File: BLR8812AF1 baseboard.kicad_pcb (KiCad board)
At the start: 2 copper layers, 38 x 38 mm, 24 parts, among them U1 MP2307DN, U2 USBLC6-2SC6, U3 BL-R8812AF1, X1 TYPE-C-31-M-12

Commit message: Working on board
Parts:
- added MH1: MountingHole, MountingHole:MountingHole_2.2mm_M2, F.Cu at (52.9, 62.2)
- added MH2: MountingHole, MountingHole:MountingHole_2.2mm_M2, F.Cu at (52.9, 28.8)
- added MH3: MountingHole, MountingHole:MountingHole_2.2mm_M2, F.Cu at (86.4, 28.8)
- added MH4: MountingHole, MountingHole:MountingHole_2.2mm_M2, F.Cu at (86.4, 62.2)
- added X2: ~, ULF:TH_1.7_1.7_1, F.Cu at (69.0, 28.2)
- added X3: ~, ULF:TH_1_1_0.65, F.Cu at (60.5, 40.3)
- added X4: ~, ULF:TH_1_1_0.65, F.Cu at (60.5, 38.4)
- added X5: ~, ULF:TH_1.7_1.7_1, F.Cu at (69.0, 35.1)
- added X6: ~, ULF:TH_1_1_0.65, F.Cu at (60.5, 42.2)
- C1, C2: value 10u -> 22u
- L1: footprint PCM_Inductor_SMD_AKL:L_7.3x7.3_H4.5 -> Inductor_SMD:L_SXN_SMDRI62
- moved U3 41.5 mm to (56.1, 61.3)
- moved R7 23.1 mm to (52.7, 57.4)
- moved C2 19.4 mm to (72.4, 31.6)
- moved U1 19.2 mm to (77.3, 30.7)
- moved C6 19.1 mm to (72.4, 28.5)
- moved C4 19.1 mm to (82.0, 28.8)
- moved R8 19.1 mm to (80.3, 34.9)
- moved C7 19.1 mm to (82.1, 31.4)
- moved C5 19.1 mm to (82.1, 32.6)
- moved C8 19.1 mm to (79.8, 39.7)
- moved R2 19.1 mm to (82.1, 30.1)
- moved R3 19.1 mm to (82.1, 33.9)
- moved R9 19.1 mm to (79.0, 34.9)
- moved L1 19.1 mm to (73.9, 38.3)
- moved C1 18.9 mm to (69.0, 31.6)
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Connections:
- net Net-(X1-DN1) renamed /DN
- net Net-(X1-DP1) renamed /DP

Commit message: Completed placing
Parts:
- moved X6 6.46 mm to (58.9, 36.0)
- moved R5 5.28 mm to (52.1, 43.2), turned to -90 degrees
- moved R4 2.98 mm to (53.6, 43.2), turned to -90 degrees
- moved D1 2.69 mm to (65.4, 37.7), turned to -90 degrees
- moved R6 1.63 mm to (65.4, 40.5), turned to -90 degrees
- moved R7 0.49 mm to (52.9, 56.9)
- moved U3 0.45 mm to (56.1, 60.8)
- moved MH1 0.40 mm to (52.6, 62.5)
- moved MH4 0.40 mm to (86.6, 62.5)
- moved MH2 0.40 mm to (52.6, 28.5)
- moved MH3 0.40 mm to (86.6, 28.5)
- moved R1 0.30 mm to (53.8, 33.0)
- moved C9 0.20 mm to (82.4, 39.7)
- moved C3 0.20 mm to (53.8, 35.5)
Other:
- outline, holes or cut-outs redrawn
- board text added: "ADD PADS FOR USB to CAM CONNECTION AND POWERRRRRR Ensure holes size"
- board text removed: "ADD PADS FOR USB to CAM CONNECTION AND POWERRRRRR"

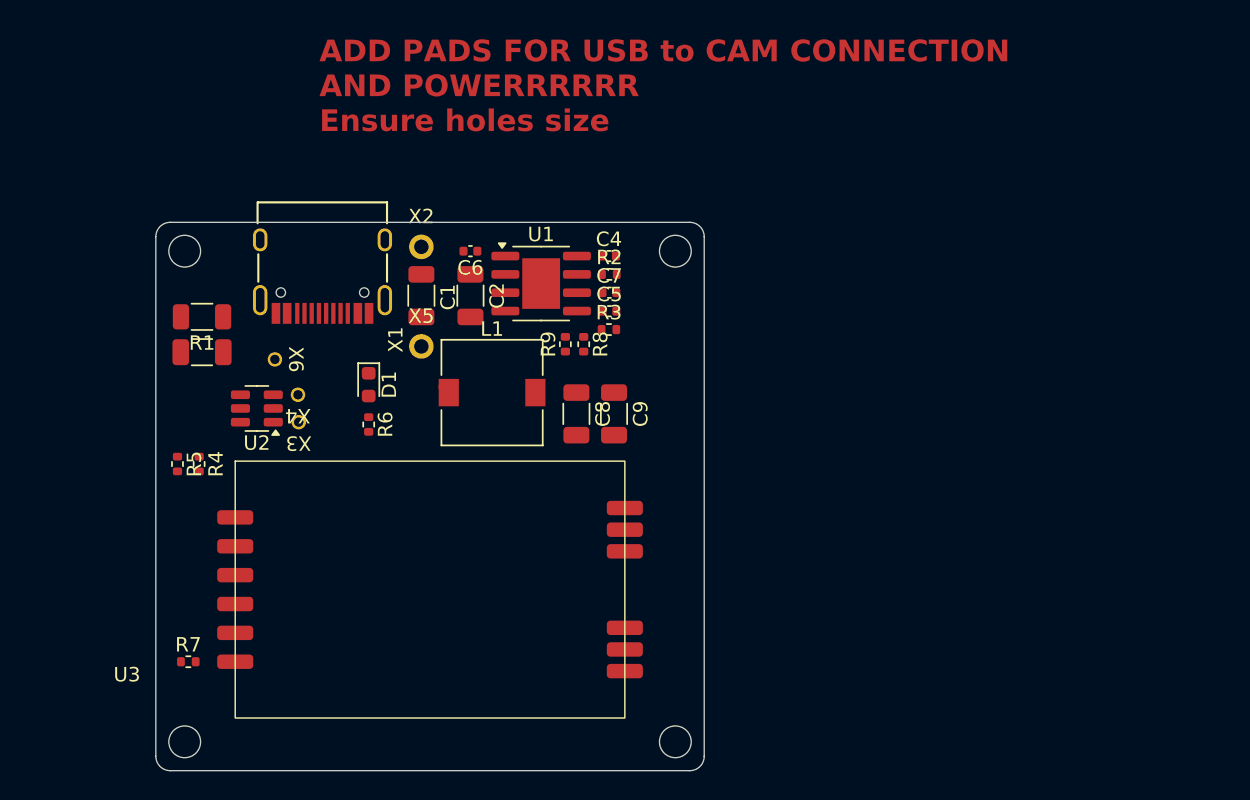
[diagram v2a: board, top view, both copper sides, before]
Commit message: changed DC-DC
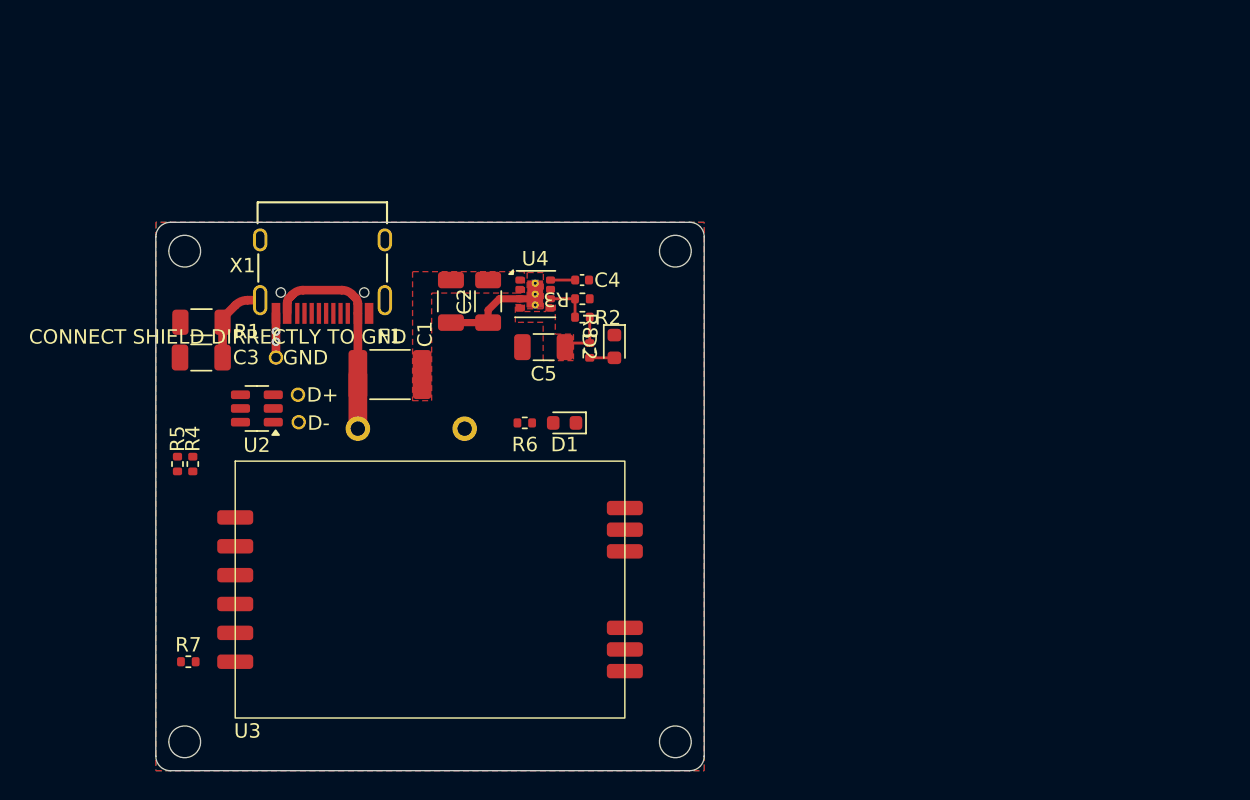
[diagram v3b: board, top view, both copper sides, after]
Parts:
- removed C6: 10n, Capacitor_SMD:C_0402_1005Metric
- removed C7: DNP, Capacitor_SMD:C_0402_1005Metric
- removed C8, C9: 22u, Capacitor_SMD:C_1206_3216Metric
- removed L1: 2uH, Inductor_SMD:L_SXN_SMDRI62
- removed R9: 10k, Resistor_SMD:R_0402_1005Metric
- removed U1: MP2307DN, Package_SO:SOIC-8-1EP_3.9x4.9mm_P1.27mm_EP2.62x3.51mm
- added D2: DNP, LED_SMD:LED_0603_1608Metric, F.Cu at (82.4, 35.1)
- added F1: MF-MSMF110-2, Fuse:Fuse_1812_4532Metric_Pad1.30x3.40mm_HandSolder, F.Cu at (66.9, 37.0)
- added U4: TPS82130, Package_LGA:Texas_SIL0008D_MicroSiP-8-1EP_2.8x3mm_P0.65mm_EP1.1x1.9mm_ThermalVias, F.Cu at (76.9, 31.4)
- C4: value 0.1u -> 430p
- C5: value 3.9n -> 22u; footprint Capacitor_SMD:C_0402_1005Metric -> Capacitor_SMD:C_1206_3216Metric
- R2: value 100k -> 309k
- R3: value 6k8 -> 100k
- R8: value 26k1 -> DNP
- moved D1 13.8 mm to (79.0, 40.4), turned to 180 degrees
- moved X2 13.3 mm to (64.6, 40.8)
- moved R6 10.8 mm to (76.2, 40.4), turned to 180 degrees
- moved X5 6.44 mm to (72.0, 40.8)
- moved C5 5.19 mm to (77.5, 35.1), turned to 180 degrees
- moved R2 3.51 mm to (80.2, 33.0)
- moved R3 2.82 mm to (80.2, 31.8), turned to 180 degrees
- moved C4 2.50 mm to (80.2, 30.5)
- moved C1 2.09 mm to (71.1, 31.9)
- moved C2 1.29 mm to (73.7, 31.9)
- moved R8 0.60 mm to (80.7, 35.3), turned to 90 degrees
- moved R4 0.44 mm to (53.2, 43.2)
- moved R1 0.38 mm to (53.8, 33.4)
- moved C3 0.37 mm to (53.8, 35.8)
- moved X6 0.15 mm to (59.0, 35.8)
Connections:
- net Net-(R4-Pad1) renamed /D1_P
- net Net-(R5-Pad1) renamed /D1_N
- net Net-(U3-DN) renamed /D2_N
- net Net-(U3-DP) renamed /D2_P
- C1 pad 1: VBUS -> /Vin
- C2 pad 1: VBUS -> /Vin
- C5 pad 1: Net-(U1-COMP) -> 3.3V
- C5 pad 2: Net-(C5-Pad2) -> GND
- R2 pad 1: Net-(U1-EN) -> Net-(U4-FB)
- R2 pad 2: VBUS -> 3.3V
- R3 pad 2: Net-(C5-Pad2) -> Net-(U4-FB)
- R8 pad 2: 3V3 -> 3.3V
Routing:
- net VBUS: track 0.00 -> 15.2 mm
- net GND: track 0.00 -> 10.2 mm, vias 0 -> 2
- net Net-(C3-Pad1): track 0.00 -> 5.80 mm
- net 3.3V: track 0.00 -> 3.63 mm
- net Net-(U4-FB): track 0.00 -> 2.97 mm
- net Net-(U4-SS/TR): track 0.00 -> 1.71 mm
- net Net-(D2-A): track 0.00 -> 1.71 mm
- added copper zone on F.Cu, net /Vin
- added copper zone on F.Cu, net 3.3V
- added copper zone on B.Cu, net GND
- added copper zone on F.Cu, net GND
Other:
- board text added: "CONNECT SHIELD DIRRECTLY TO GND"
- board text added: "D+"
- board text added: "D-"
- board text added: "GND"
- board text removed: "ADD PADS FOR USB to CAM CONNECTION AND POWERRRRRR Ensure holes size"

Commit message: almost done
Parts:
- removed the C3 at (53.8, 35.8)
- added C5: 22u, Capacitor_SMD:C_1206_3216Metric, F.Cu at (53.3, 56.4)
- added Q1: AO3401A, Package_TO_SOT_SMD:SOT-23, F.Cu at (72.3, 37.0)
- R1: value 1M -> 10k; footprint Resistor_SMD:R_1206_3216Metric -> Resistor_SMD:R_0402_1005Metric
- moved R1 22.4 mm to (75.7, 38.0), turned to 90 degrees
- moved D1 18.7 mm to (60.3, 38.7)
- moved R4 18.7 mm to (57.6, 38.7)
- moved R5 9.37 mm to (60.5, 62.4), turned to 180 degrees
- moved X3 8.33 mm to (53.4, 34.0), turned to -90 degrees
- moved X2 8.19 mm to (55.3, 34.0), turned to -90 degrees
- moved U1 3.99 mm to (54.4, 37.1), turned to -90 degrees
- moved X4 2.52 mm to (57.2, 34.0)
- moved R3 1.77 mm to (52.5, 45.0)
- moved R2 1.77 mm to (53.5, 45.0)
- renumbered C4 to C3, C5 to C4, R4 to R2, R5 to R3, R6 to R4, R7 to R5, R3 to R6, R2 to R7, U2 to U1, U3 to U2, U4 to U3, X3 to X2, X4 to X3, X6 to X4, X2 to X5, X5 to X6
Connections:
- net VBUS renamed +VBUS
- C4 pad 1: 3.3V -> +3.3V
- F1 pad 2: /Vin -> Net-(Q1-S)
- R1 pad 1: Net-(C3-Pad1) -> GND
- R1 pad 2: GND -> Net-(Q1-G)
- R7 pad 2: 3.3V -> +3.3V
- R8 pad 2: 3.3V -> +3.3V
- U2 pad 2: 3V3 -> +3.3V
- U3 pad 4: 3.3V -> +3.3V
- U3 pad 5: 3.3V -> +3.3V
- X1 pad SHIELD: Net-(C3-Pad1) -> GND
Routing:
- net +3.3V: track 0.00 -> 51.7 mm, vias 0 -> 4
- net /DN: track 0.00 -> 18.1 mm
- net /DP: track 0.00 -> 17.5 mm
- net /D2_N: track 0.00 -> 9.97 mm
- net /D2_P: track 0.00 -> 9.26 mm
- net /Vin: track 0.00 -> 8.87 mm, vias 0 -> 5
- net +VBUS: track 15.2 -> 24.0 mm
- net /D1_P: track 0.00 -> 7.25 mm
- net /D1_N: track 0.00 -> 7.25 mm
- net Net-(C3-Pad1): track 5.80 -> 0.00 mm
- net Net-(Q1-G): track 0.00 -> 3.68 mm
- net 3.3V: track 3.63 -> 0.00 mm
- net GND: track 10.2 -> 10.9 mm, vias 2 -> 6
- added copper zone on F.Cu, net +3.3V
- added copper zone on F.Cu, net Net-(Q1-S)
- removed copper zone on F.Cu, net 3.3V
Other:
- board text added: "+5V"
- board text removed: "CONNECT SHIELD DIRRECTLY TO GND"

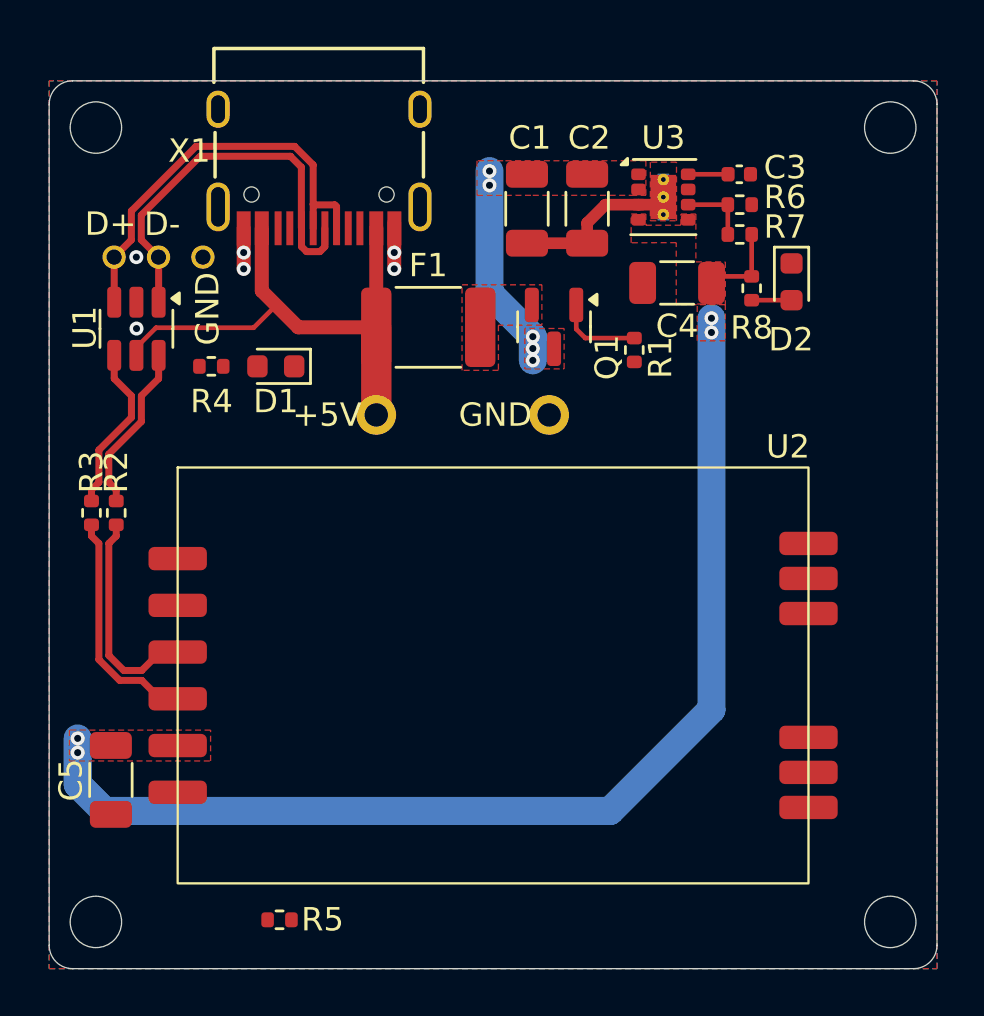
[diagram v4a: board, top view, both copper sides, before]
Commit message: Done placing and routing, need to add stiching vias
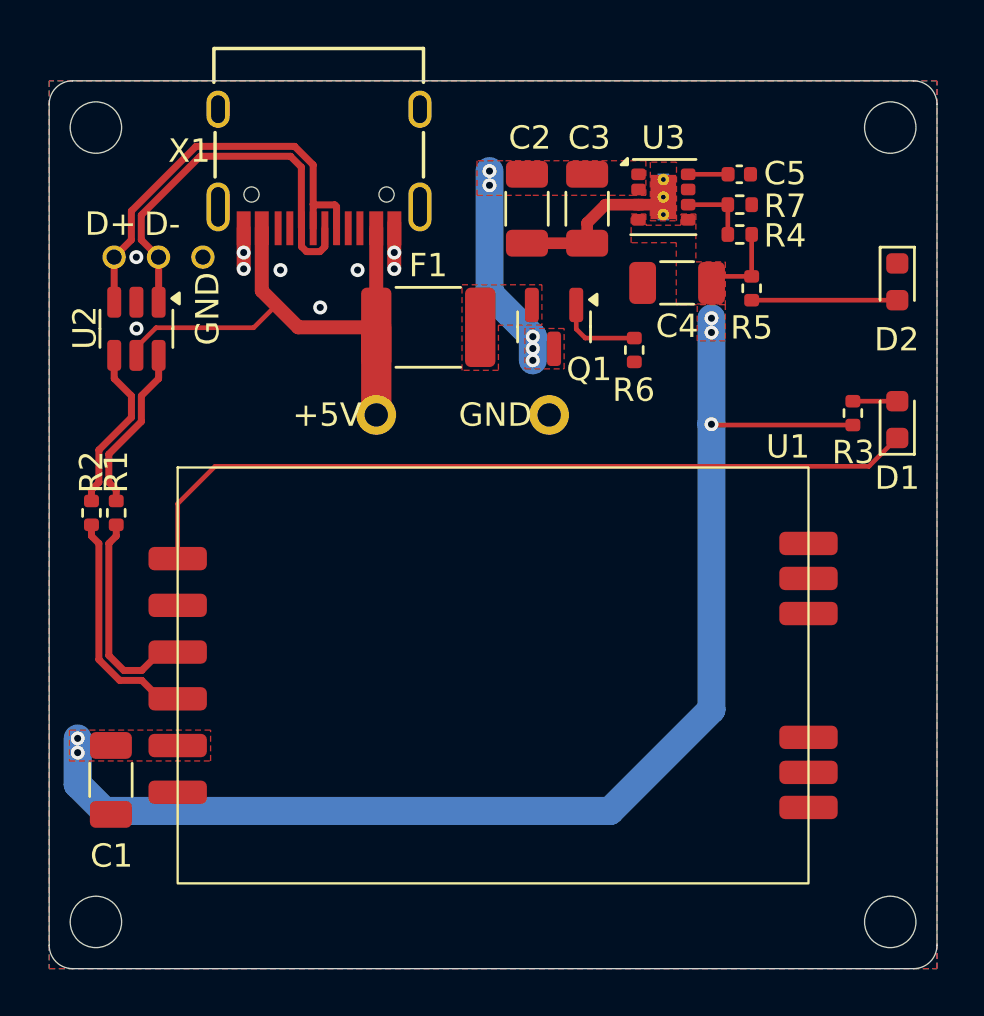
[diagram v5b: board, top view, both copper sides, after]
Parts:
- removed the R5 at (60.5, 62.4)
- moved R3 27.5 mm to (85.0, 40.7), turned to -90 degrees
- moved D1 26.7 mm to (86.9, 41.0), turned to 90 degrees
- moved D2 4.52 mm to (86.9, 35.1)
- renumbered C5 to C1, C1 to C2, C2 to C3, C3 to C5, R2 to R1, R3 to R2, R4 to R3, R7 to R4, R8 to R5, R1 to R6, R6 to R7, U2 to U1, U1 to U2, X5 to X4, X4 to X5
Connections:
- D1 pad 1: GND -> Net-(D1-K)
- R3 pad 2: Net-(U2-LED) -> +3.3V
- U1 pad 1: Net-(U2-PDN) -> unconnected-(U1-PDN-Pad1)
- U1 pad 6: Net-(U2-LED) -> Net-(D1-K)
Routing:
- net Net-(D1-K): track 0.00 -> 34.3 mm
- net +3.3V: track 51.7 -> 57.8 mm, vias 4 -> 5
- net Net-(D2-A): track 1.71 -> 6.23 mm
- net Net-(D1-A): track 0.00 -> 1.90 mm
- net GND: vias 6 -> 9

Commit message: PCB done
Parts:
- R3, R5: value DNP -> 1k
- U3: footprint Package_LGA:Texas_SIL0008D_MicroSiP-8-1EP_2.8x3mm_P0.65mm_EP1.1x1.9mm_ThermalVias -> Package_LGA:Texas_SIL0008D_MicroSiP-8-1EP_2.8x3mm_P0.65mm_EP1.1x1.9mm
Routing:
- net GND: vias 9 -> 12

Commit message: DONE
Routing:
- net GND: vias 12 -> 138

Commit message: Fixed reverce voltage protection
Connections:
- F1 pad 2: Net-(Q1-S) -> Net-(Q1-D)
- Q1 pad 2: Net-(Q1-S) -> /Vin
- Q1 pad 3: /Vin -> Net-(Q1-D)
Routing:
- net /DN: track 18.1 -> 19.1 mm
- added copper zone on F.Cu, net Net-(Q1-D)
- removed copper zone on F.Cu, net Net-(Q1-S)
